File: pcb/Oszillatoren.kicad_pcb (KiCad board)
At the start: 2 copper layers, 100 x 55 mm, 67 parts, among them J1 Conn_01x01_Pin, J10 Conn_01x01_Pin, J11 Conn_01x01_Pin, J12 Conn_01x01_Pin, J13 Conn_01x01_Pin, J14 Conn_01x01_Pin, J15 Conn_01x01_Pin, J16 Conn_01x01_Pin, J17 Conn_01x01_Pin, J18 Conn_01x01_Pin, J19 Conn_01x01_Pin, J2 Conn_01x01_Pin, J3 Conn_01x01_Pin, J4 Conn_01x01_Pin, J5 Conn_01x01_Pin, J6 Conn_01x01_Pin, J7 Conn_01x01_Pin, J8 Conn_01x01_Pin, J9 Conn_01x01_Pin, U1 74AHC1G4210, U2 40106, U3 LM358, U4 LM358, Y1 Crystal, Y2 Crystal

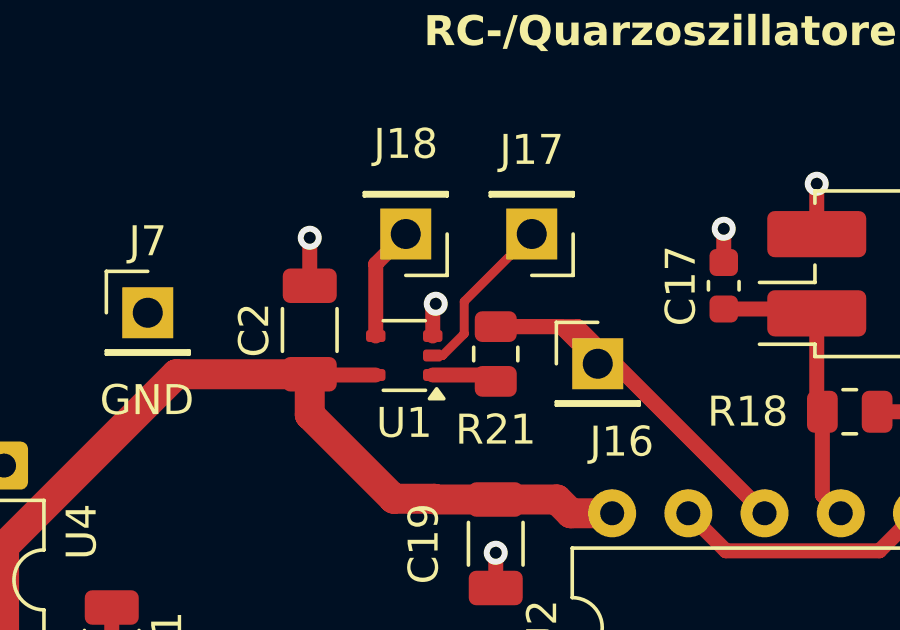
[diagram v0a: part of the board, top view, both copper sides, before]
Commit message: Bibliotheken aktualisiert
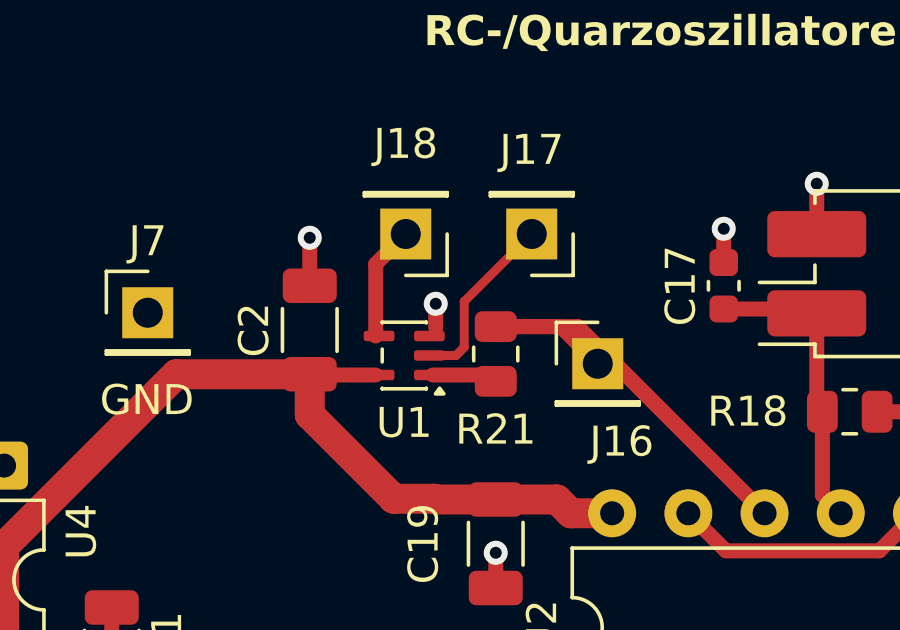
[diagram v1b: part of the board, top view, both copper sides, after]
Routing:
- net Net-(J17-Pin_1): track 5.61 -> 6.31 mm
